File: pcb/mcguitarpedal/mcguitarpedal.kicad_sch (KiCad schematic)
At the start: 40 parts, among them J1 IN, J2 PREAMP_HEADERS, J3 BTN_MTX, J4 OUT, J5 EXP, J6 ILI9488 Module, J7 PWR_IN, J8 POT_HP_VOLUME_10k, SW1 SW_BYPASS, SW2 SW_TUNER, SW3 SW_PRESET, U1 Teensy4.0_AudioShield_REVD, U2 Teensy4.1, U4 74HC148, U5 74HC4094, U6 STPDWN-3P-5V, U7 STDN-3A24-ADJ

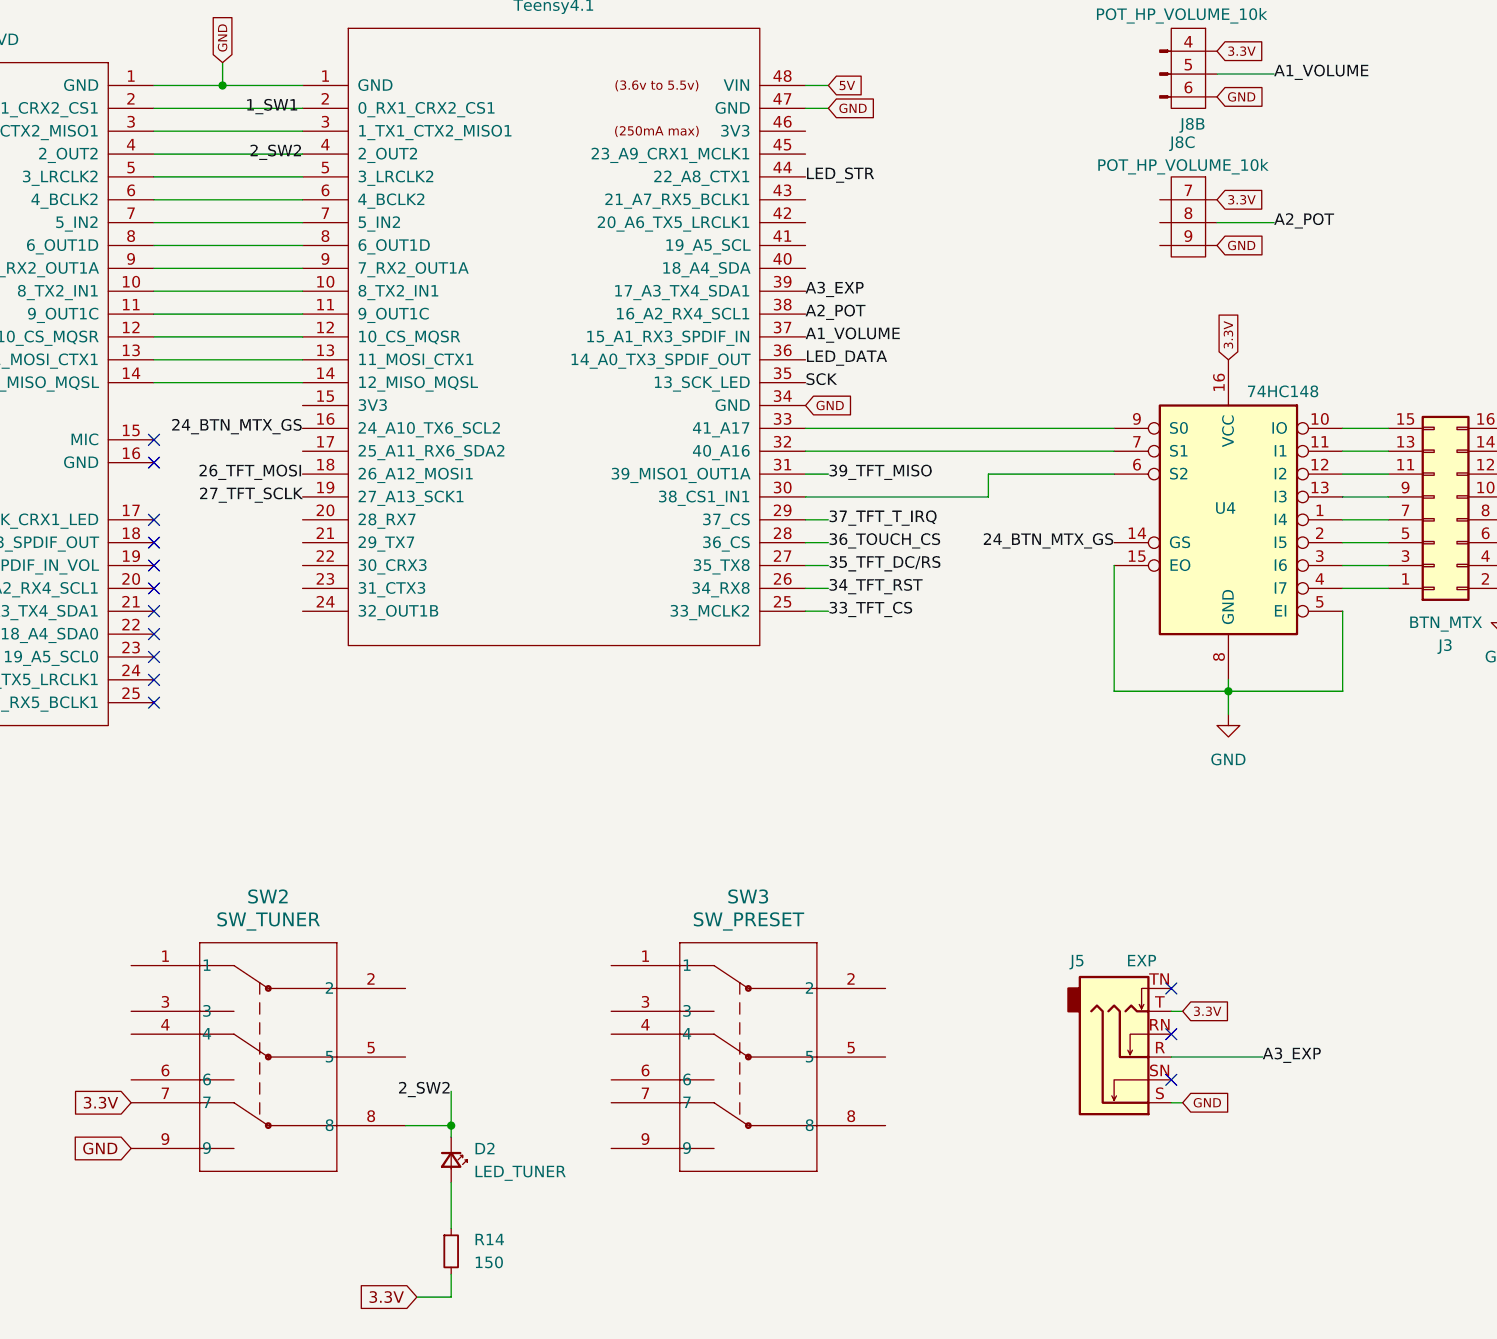
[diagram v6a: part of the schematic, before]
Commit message: Encoder headers
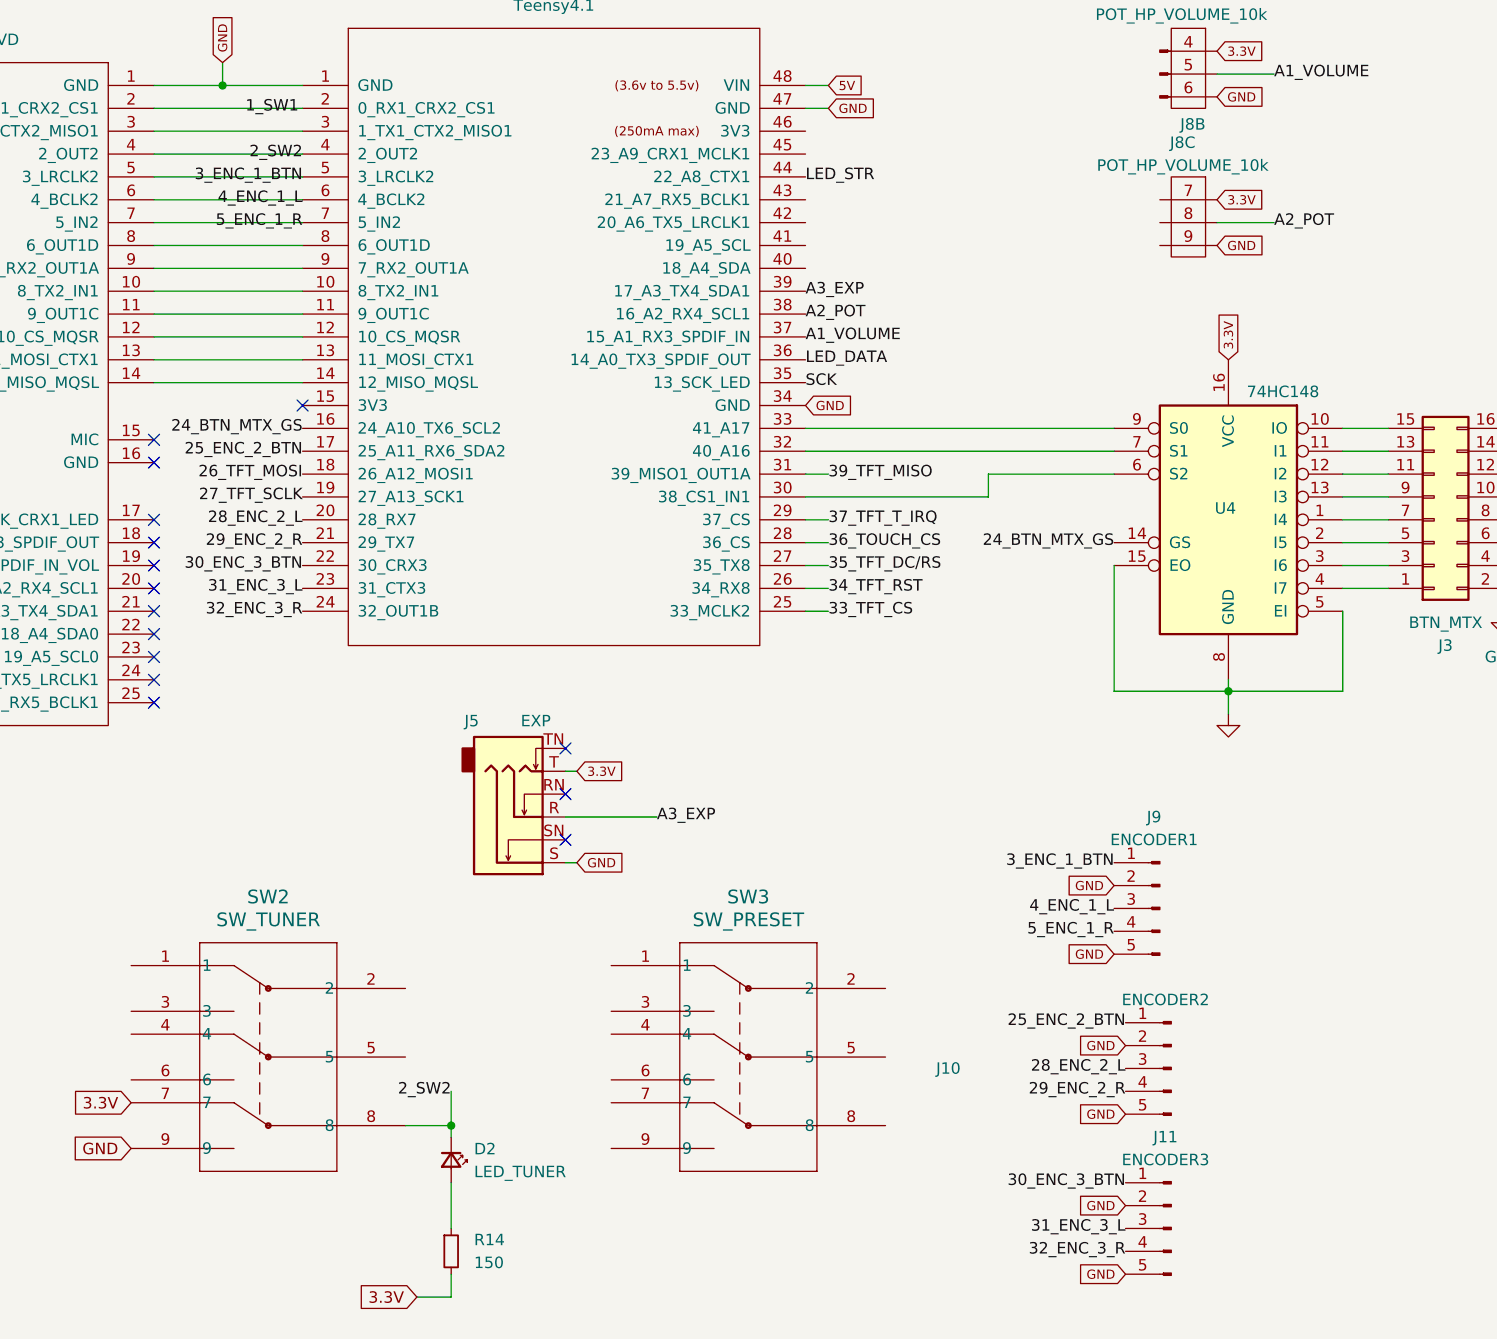
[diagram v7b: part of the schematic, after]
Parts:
- added J10: ENCODER2, Connector_PinHeader_2.54mm:PinHeader_1x05_P2.54mm_Vertical, symbol Connector:Conn_01x05_Pin
- added J11: ENCODER3, Connector_PinHeader_2.54mm:PinHeader_1x05_P2.54mm_Vertical, symbol Connector:Conn_01x05_Pin
- added J9: ENCODER1, Connector_PinHeader_2.54mm:PinHeader_1x05_P2.54mm_Vertical, symbol Connector:Conn_01x05_Pin
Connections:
- net GND: now also J10.2 (Pin_2), J10.5 (Pin_5), J11.2 (Pin_2), J11.5 (Pin_5), J9.2 (Pin_2), J9.5 (Pin_5)
- net 3_ENC_1_BTN: now reaches U1.5 (3_LRCLK2), U2.5 (3_LRCLK2)
- net 3_ENC_1_BTN: now also J9.1 (Pin_1)
- net 4_ENC_1_L: now reaches U1.6 (4_BCLK2), U2.6 (4_BCLK2)
- net 4_ENC_1_L: now also J9.3 (Pin_3)
- net 5_ENC_1_R: now reaches U1.7 (5_IN2), U2.7 (5_IN2)
- net 5_ENC_1_R: now also J9.4 (Pin_4)
- net 25_ENC_2_BTN: now reaches U2.17 (25_A11_RX6_SDA2)
- net 25_ENC_2_BTN: now also J10.1 (Pin_1)
- net 28_ENC_2_L: now reaches U2.20 (28_RX7)
- net 28_ENC_2_L: now also J10.3 (Pin_3)
- net 29_ENC_2_R: now reaches U2.21 (29_TX7)
- net 29_ENC_2_R: now also J10.4 (Pin_4)
- net 30_ENC_3_BTN: now reaches U2.22 (30_CRX3)
- net 30_ENC_3_BTN: now also J11.1 (Pin_1)
- net 31_ENC_3_L: now reaches U2.23 (31_CTX3)
- net 31_ENC_3_L: now also J11.3 (Pin_3)
- net 32_ENC_3_R: now reaches U2.24 (32_OUT1B)
- net 32_ENC_3_R: now also J11.4 (Pin_4)
- no-connect marks 33 -> 34
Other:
- moved on the sheet: J5

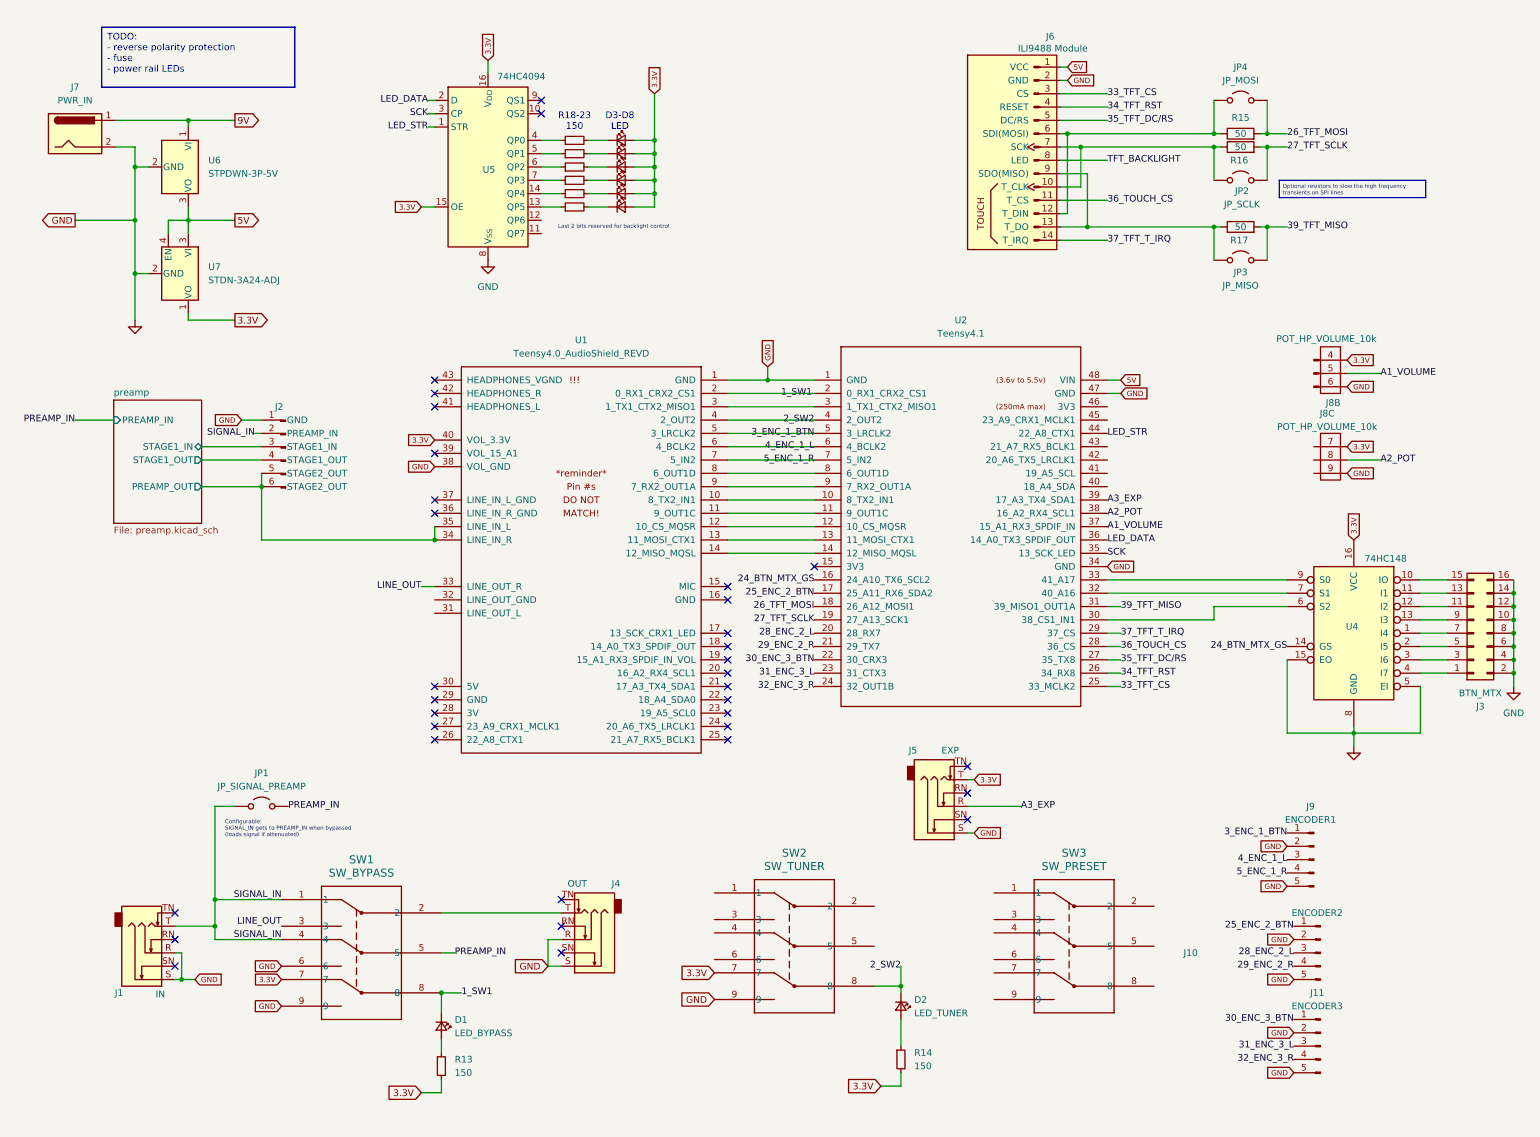
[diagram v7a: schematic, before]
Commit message: Changed to DPDT switches
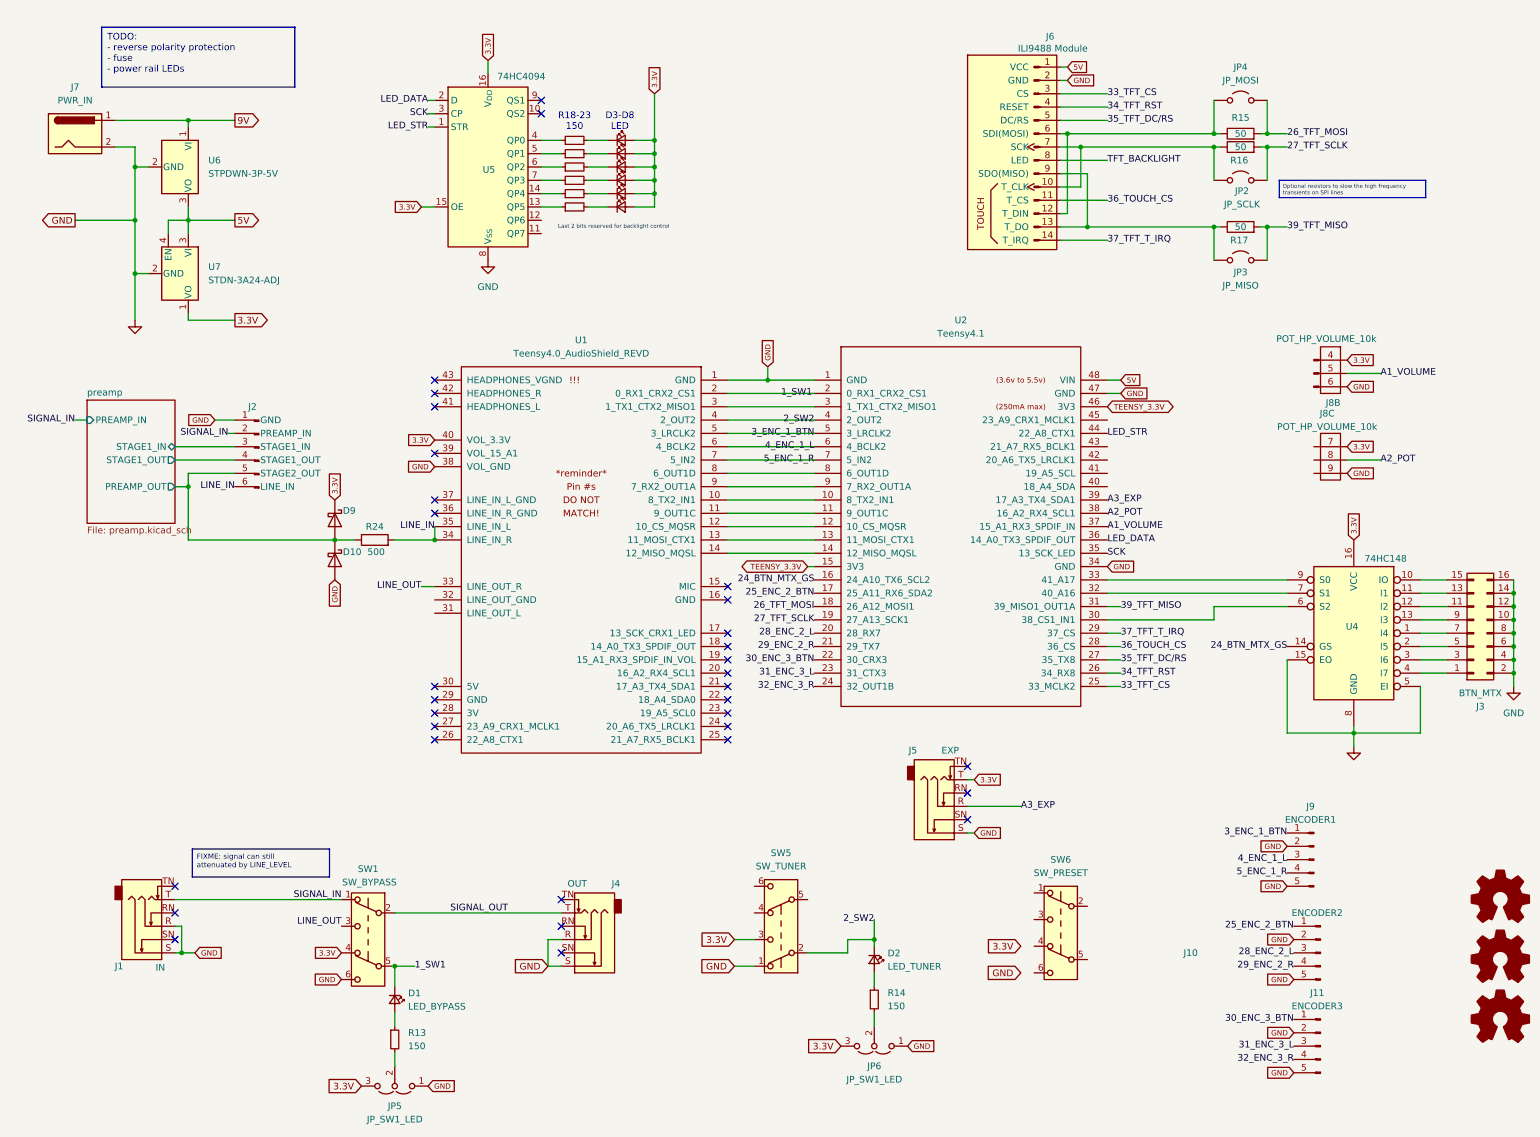
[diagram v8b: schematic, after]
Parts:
- removed JP1: JP_SIGNAL_PREAMP, Connector_PinHeader_2.54mm:PinHeader_1x02_P2.54mm_Vertical, symbol Jumper:Jumper_2_Open
- removed SW1: SW_BYPASS, TI_FOOTPRINTS:01-690DB_3PDT_JCV_OVAL, symbol 3PDT_FOOT_SWITCH:01-690DB-RH
- removed SW2: SW_TUNER, TI_FOOTPRINTS:01-690DB_3PDT_JCV_OVAL, symbol 3PDT_FOOT_SWITCH:01-690DB-RH
- removed SW3: SW_PRESET, TI_FOOTPRINTS:01-690DB_3PDT_JCV_OVAL, symbol 3PDT_FOOT_SWITCH:01-690DB-RH
- added D10, D9: D_Schottky, TI_FOOTPRINTS:DO-41_DIO, symbol Device:D_Schottky
- added JP5, JP6: JP_SW1_LED, Connector_PinHeader_2.54mm:PinHeader_1x03_P2.54mm_Vertical, symbol Jumper:Jumper_3_Open
- added POT1, POT2, POT3: Logo_Open_Hardware_Small, mcguitarpedal:Floating Potentiometer, symbol Graphic:Logo_Open_Hardware_Small
- added R24: 500, Resistor_THT:R_Axial_DIN0207_L6.3mm_D2.5mm_P7.62mm_Horizontal, symbol Device:R
- added SW1: SW_BYPASS, mcguitarpedal:SW_PUSH_DPDT, symbol Switch:SW_Push_DPDT
- added SW5: SW_TUNER, mcguitarpedal:SW_PUSH_DPDT, symbol Switch:SW_Push_DPDT
- added SW6: SW_PRESET, mcguitarpedal:SW_PUSH_DPDT, symbol Switch:SW_Push_DPDT
- U2: footprint mcguitarpedal:PinHeader_2x24_P2.54mm_W15.24_Vertical -> mcguitarpedal:Teensy 4.1 with audio board
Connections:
- net 1_SW1: now also SW1.5 (B)
- net 2_SW2: now also SW5.2 (B)
- net 3.3V: now also D9.1 (K), JP5.3 (B), JP6.3 (B), SW1.4 (A), SW5.3 (C); no longer R13.2, R14.2
- net GND: now also D10.2 (A), JP5.1 (A), JP6.1 (A), SW1.6 (C), SW5.1 (A)
- net LINE_OUT: now also SW1.3 (C)
- net SIGNAL_IN: now also SW1.1 (A)
- net preamp/PREAMP_OUT: now also D10.1 (K), D9.2 (A), R24.1; no longer J2.6 (STAGE2_OUT), U1.34 (LINE_IN_R), U1.35 (LINE_IN_L)
- net SIGNAL_OUT: now reaches J4.T
- net SIGNAL_OUT: now also SW1.2 (B)
- net TEENSY_3.3V: now reaches U2.15 (3V3)
- net TEENSY_3.3V: now also U2.46 (3V3)
- new net: JP6.2 (C), R14.2
- new net: JP5.2 (C), R13.2
- new net LINE_IN: J2.6 (LINE_IN), R24.2, U1.34 (LINE_IN_R), U1.35 (LINE_IN_L)
- no-connect marks 34 -> 33
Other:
- moved on the sheet: D1, D2, J1, J2, R13, R14
